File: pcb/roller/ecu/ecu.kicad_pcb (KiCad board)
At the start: 4 copper layers, 187.6 x 139.6 mm, 278 parts, among them J1 SWD, J2 NTC, J3 SS-12400-004, J4 NTC, J6 TE-776163-1, J7 TE-776087-1, K1 Relay_SPDT, K10 Relay_SPST-NO, K11 Relay_SPDT, K12 Relay_SPST-NO, K13 Relay_SPDT, K14 Relay_SPST-NO, K15 Relay_SPST-NO, K16 Relay_SPST-NO, K17 Relay_SPST-NO, K18 Relay_SPST-NO, K19 Relay_SPST-NO, K2 Relay_SPDT, K20 Relay_SPST-NO, K21 Relay_SPST-NO, K22 Relay_SPST-NO, K23 Relay_SPST-NO, K24 Relay_SPDT, K25 Relay_SPST-NO, K26 Relay_SPST-NO, K27 Relay_SPST-NO, K3 Relay_SPDT, K4 Relay_SPST-NO, K5 Relay_SPDT, K6 Relay_SPST-NO, K7 Relay_SPDT, K8 Relay_SPST-NO, K9 Relay_SPDT, Q1 BSN20, Q2 NVD5C684NLT4G, Q3 NVD5C684NLT4G, Q4 BC817, Q5 BSC065N06LS5, Q6 2N7002KQ-7, Q9 BSN20, SW1 SW_Push, T201 SM91071AL-E, U1 STM32H563ZITx, U10 UCC27517AQDBVRQ1, U11 UCC27517AQDBVRQ1, U12 INA240A1D, U13 SN65HVD230, U14 SN65HVD230, U15 ACPL-214-500E, U2 LM74700, U221 ATECC608C-SSHDA-T, U300 SN74AHCT541QPWRQ1, U301 TPIC6A595DWR, U302 TPIC6A595DWR, U303 TPIC6A595DWR, U304 TPIC6A595DWR, U4 LAN8742A, U5 USBLC6-4SC6, U6 INA240A1D, U7 SN74LVC1G14DBV, U8 MPQ4371GVE-1000-AEC1-P, U9 MPQ2178GQHE-AEC1-Z, Y1 32.768kHz, Y2 25MHz, Y3 25MHz

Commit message: Implement code changes to enhance functionality and improve performance
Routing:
- net +12V: track 278.3 -> 277.5 mm
- net PGND: vias 95 -> 93
- net /05_Relay_Drivers/TPIC5_SER: vias 3 -> 2

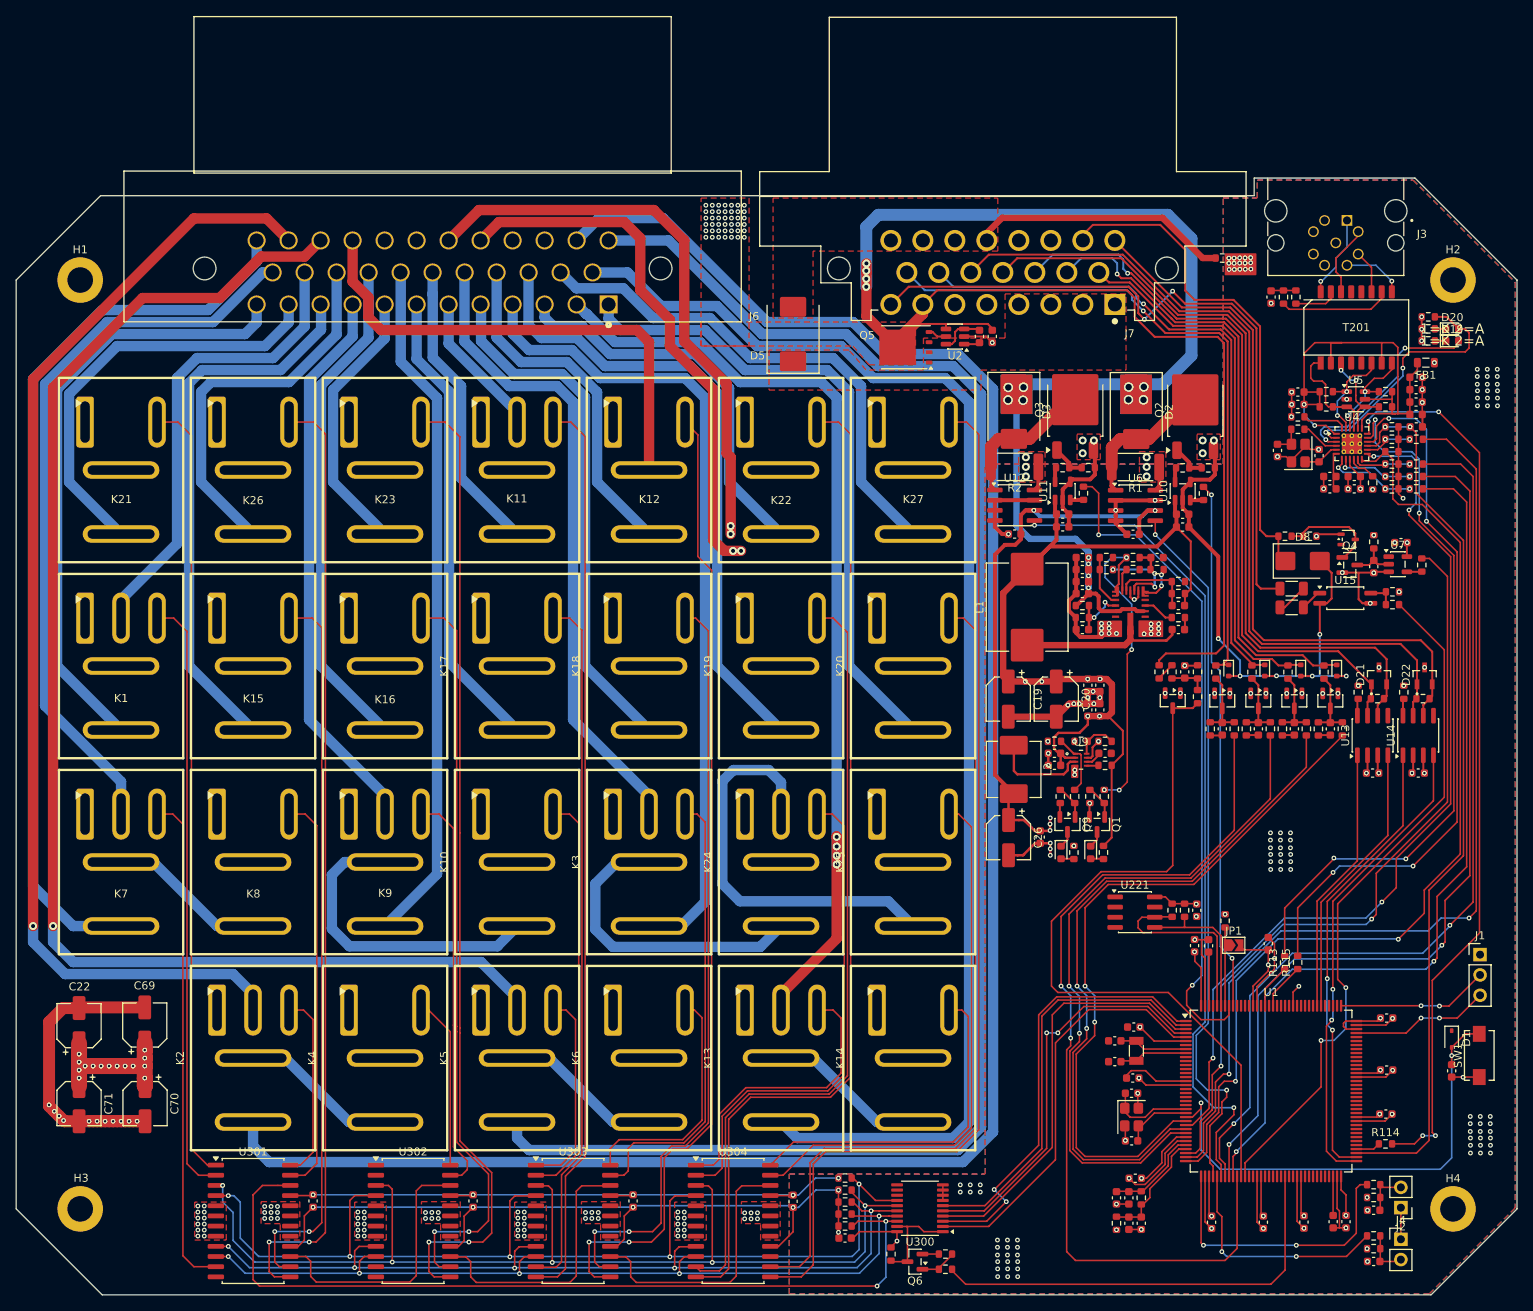
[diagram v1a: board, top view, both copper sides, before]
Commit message: Change silk edge clearance rule from warning to error in ECU PCB design
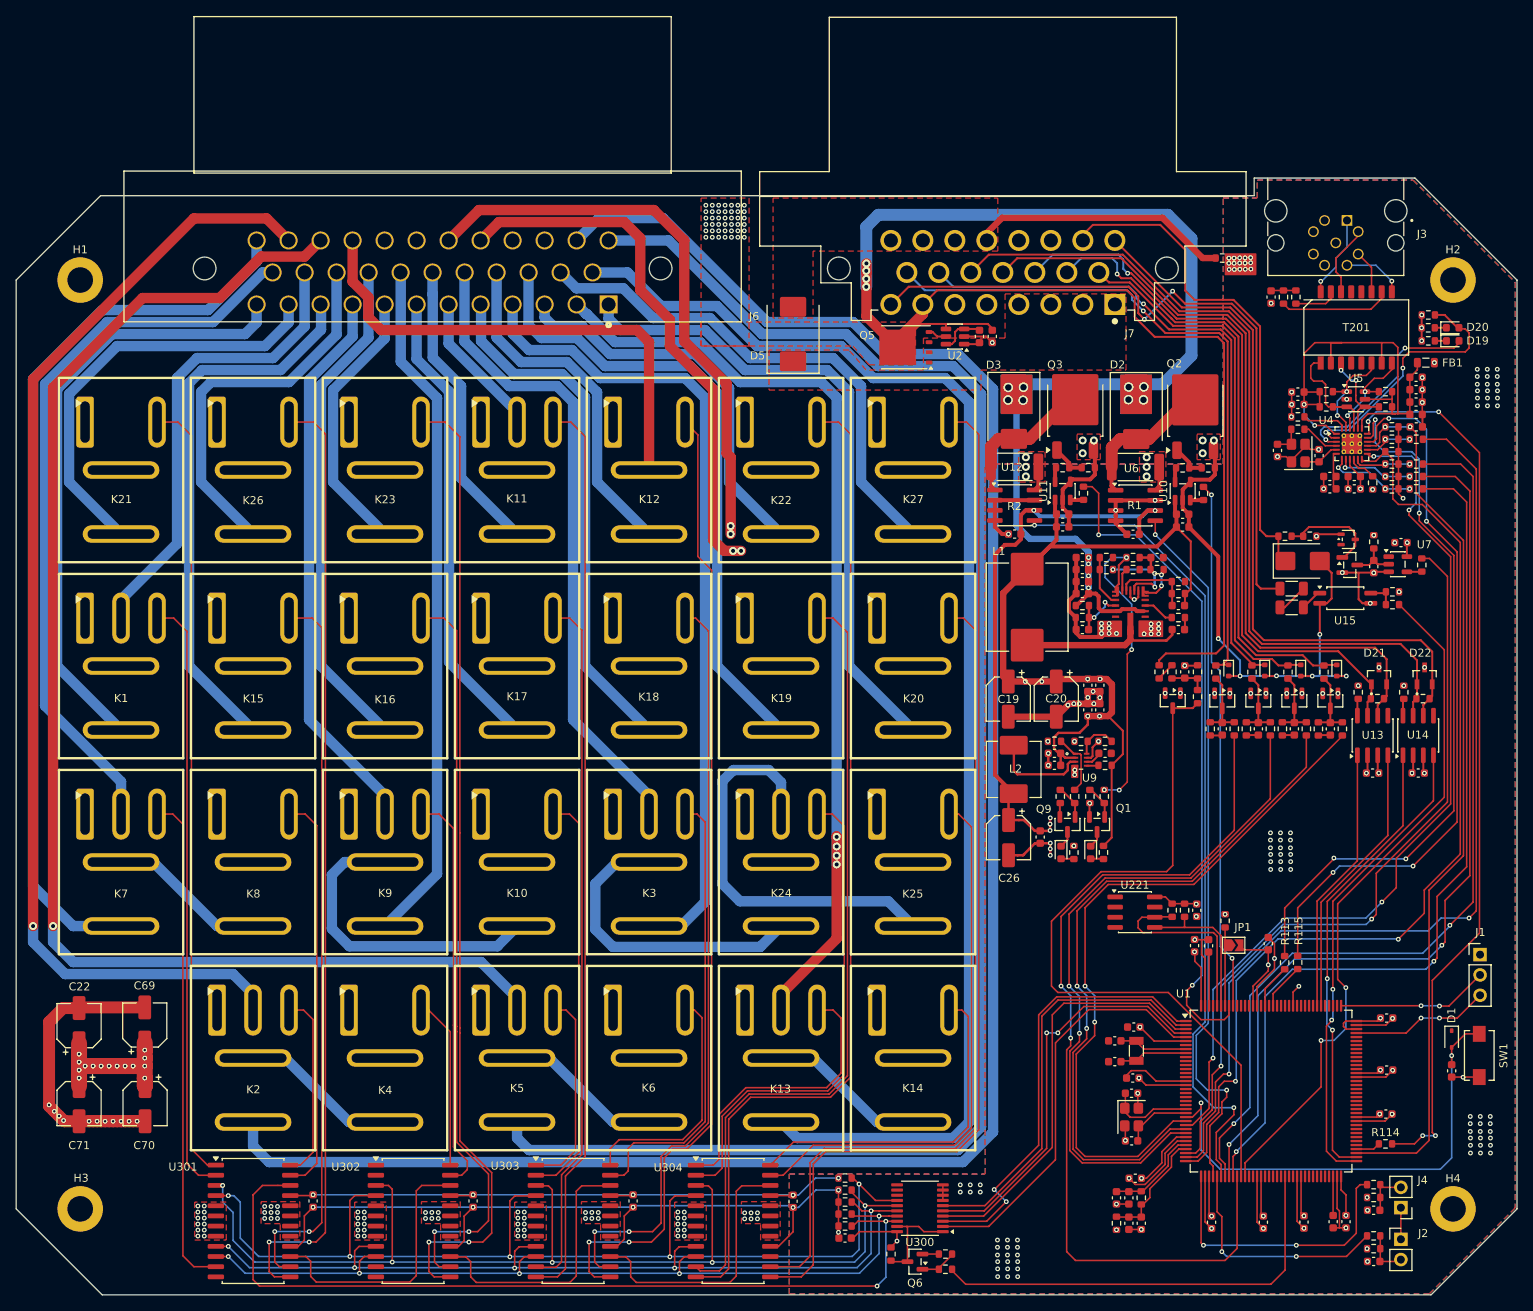
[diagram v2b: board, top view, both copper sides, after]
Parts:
- moved R56 0.24 mm to (278.9, 96.1)
- moved D20 0.15 mm to (281.9, 97.7)
- moved R57 0.13 mm to (278.9, 97.7)
- moved D19 0.06 mm to (282.0, 99.3)
